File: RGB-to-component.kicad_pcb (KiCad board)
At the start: 2 copper layers, 50 x 70 mm, 59 parts, among them J1 VGA, J3 USB_C_Receptacle_Power, J4 SCART_CONN, J5 3xRCA_CONN, U1 SC6206B-65K5, U2 THS7374, U3 RS8752XK, U6 74AHCT1G86, U7 74AHCT1G86, U8 LM1881

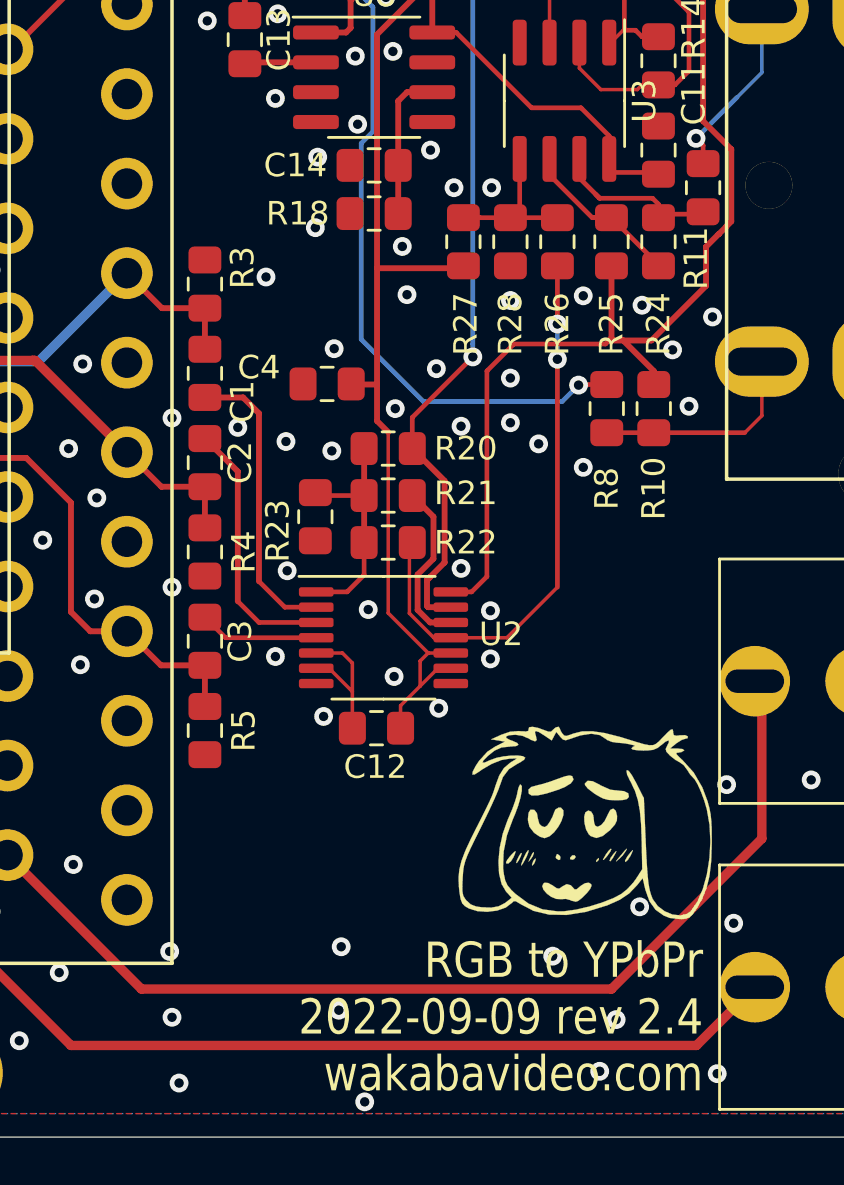
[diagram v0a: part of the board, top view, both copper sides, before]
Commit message: swapping video amps again to TPF141 for JLC availability
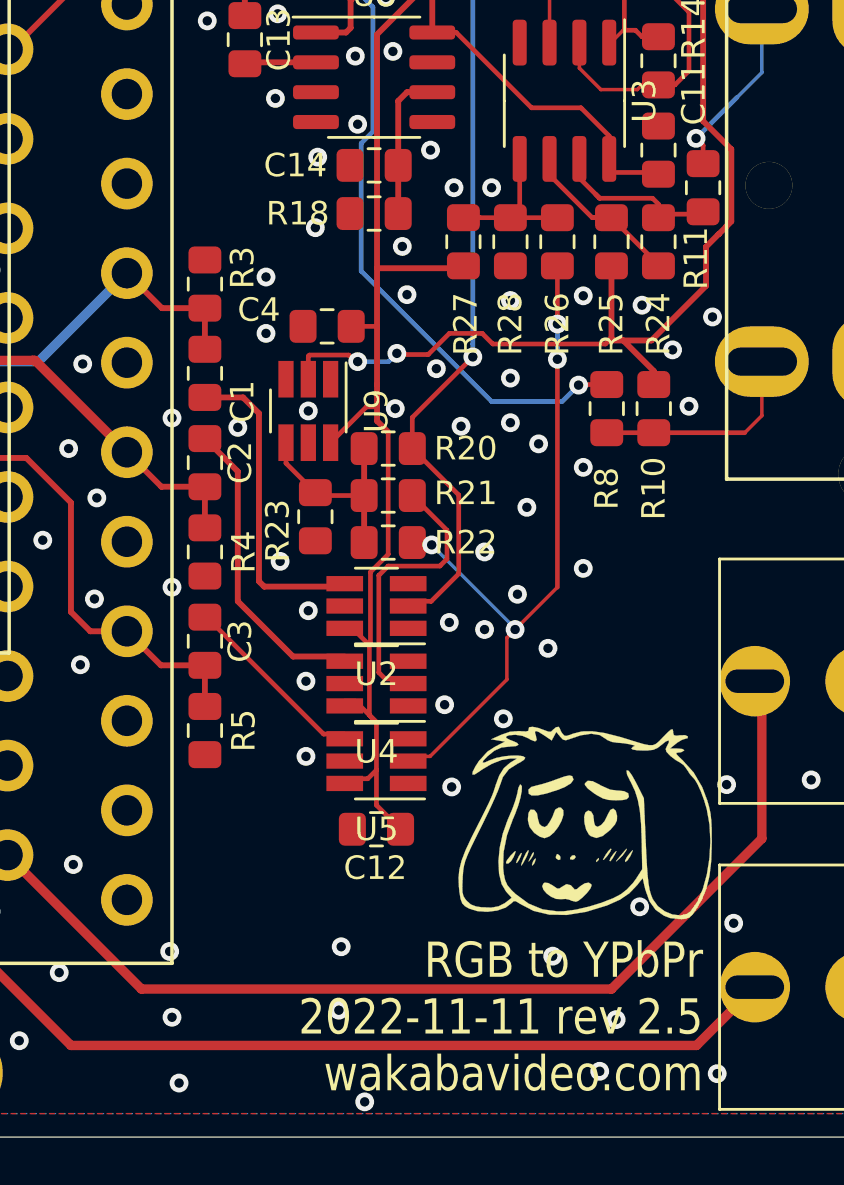
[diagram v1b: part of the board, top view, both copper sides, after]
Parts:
- added U4: TPF141-TR, Package_TO_SOT_SMD:SOT-23-6_Handsoldering, F.Cu at (45.0, 90.7)
- added U5: TPF141-TR, Package_TO_SOT_SMD:SOT-23-6_Handsoldering, F.Cu at (45.0, 94.0)
- added U9: TPF141-TR, Package_TO_SOT_SMD:SOT-23-6_Handsoldering, F.Cu at (42.1, 79.1)
- U2: value THS7374 -> TPF141-TR; footprint Package_SO:TSSOP-14_4.4x5mm_P0.65mm -> Package_TO_SOT_SMD:SOT-23-6_Handsoldering
- moved C12 4.30 mm to (45.0, 96.9)
- moved C4 2.45 mm to (42.9, 75.5)
- moved U2 1.38 mm to (45.0, 87.4), turned to 180 degrees
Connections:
- U2 pad 1: Net-(R20-Pad1) -> (no net)
- U2 pad 2: Net-(C1-Pad1) -> /2R
- U2 pad 3: Net-(C2-Pad1) -> (no net)
- U2 pad 4: Net-(C3-Pad1) -> Net-(C1-Pad1)
- U2 pad 6: GND -> VCC
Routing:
- net VCC: track 110.5 -> 119.6 mm
- net GND: track 5.89 -> 0.00 mm, vias 104 -> 108
- net /2B: track 24.4 -> 30.2 mm, vias 2 -> 4
- net /2G: track 7.15 -> 12.0 mm
- net Net-(C3-Pad1): track 5.10 -> 8.01 mm
- net Net-(C2-Pad1): track 11.2 -> 13.0 mm
- net /SYNC: track 32.9 -> 31.2 mm
- net /2Y: track 44.4 -> 42.8 mm, vias 0 -> 2
- net Net-(R20-Pad1): track 9.84 -> 8.77 mm
- net Net-(C1-Pad1): track 12.6 -> 13.6 mm
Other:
- board text added: "RGB to YPbPr 2022-11-11 rev 2.5 wakabavideo.com"
- board text removed: "RGB to YPbPr 2022-09-09 rev 2.4 wakabavideo.com"

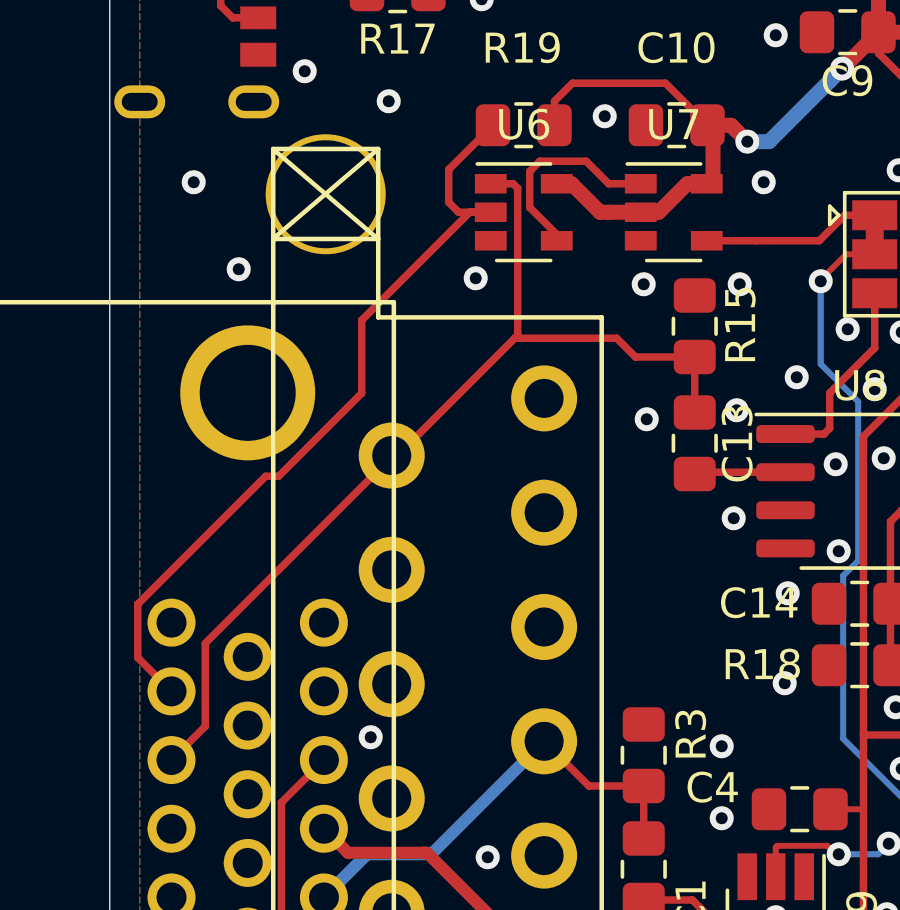
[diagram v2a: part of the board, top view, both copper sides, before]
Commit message: 75 ohm removed from hsync, only terminates scart's csync
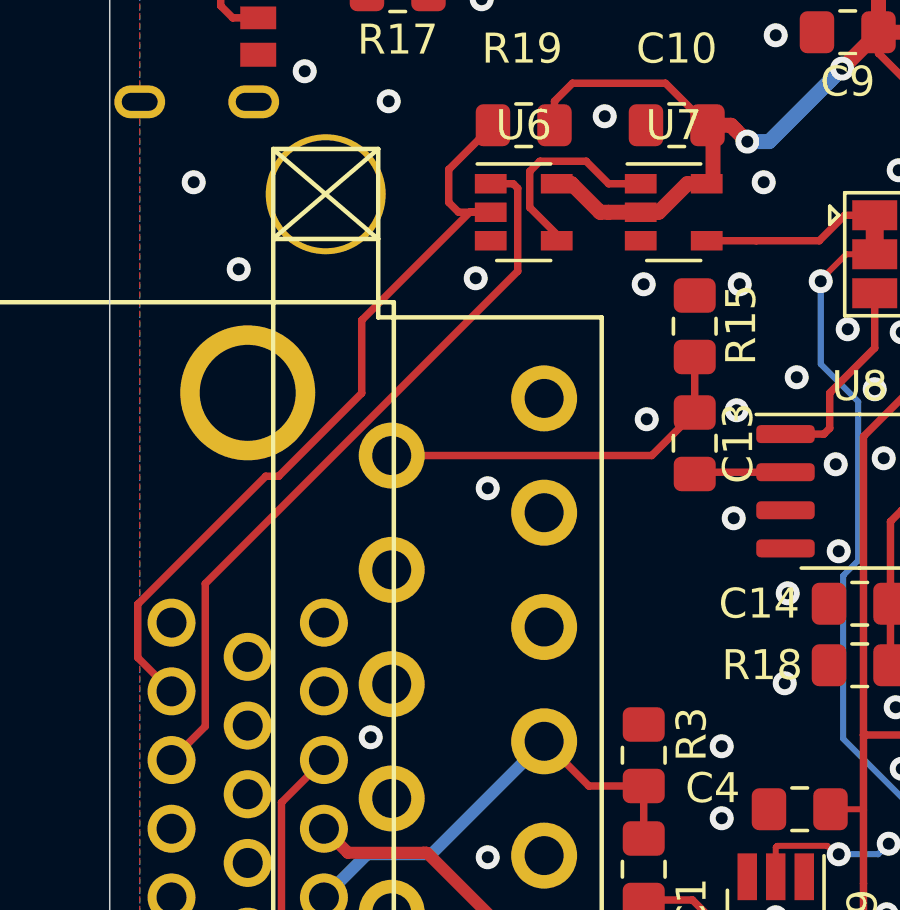
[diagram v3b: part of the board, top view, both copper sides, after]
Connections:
- C13 pad 1: /HSYNC -> /CSYNC
- J4 pad 20: /HSYNC -> /CSYNC
- R15 pad 1: /HSYNC -> /CSYNC
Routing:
- net /CSYNC: track 0.00 -> 12.7 mm
- net /HSYNC: track 33.3 -> 25.0 mm
- net GND: vias 108 -> 109

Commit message: buffer csync stripper, logic moved to single chip
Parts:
- removed U6, U7: 74AHCT1G86, Package_TO_SOT_SMD:SOT-23-5
- added U10: 74HC86, Package_SO:TSSOP-14_4.4x5mm_P0.65mm, F.Cu at (36.8, 53.4)
- moved C10 5.08 mm to (35.8, 48.6), turned to 0 degrees
- moved JP1 2.76 mm to (43.4, 55.1)
- moved R19 1.00 mm to (33.1, 53.5), turned to -90 degrees
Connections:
- JP1 pad 2: /SYNC -> Net-(JP1-C)
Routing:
- net Net-(JP1-C): track 0.00 -> 11.6 mm
- net /SYNC: track 31.2 -> 39.5 mm
- net Net-(U6-Pad4): track 6.71 -> 0.00 mm
- net Net-(U10-Pad3): track 0.00 -> 2.77 mm
- net VCC: track 119.6 -> 122.2 mm, vias 2 -> 1
- net /VGA_CSYNC: track 5.74 -> 8.20 mm
- net /STRIP_CSYNC: track 6.68 -> 7.96 mm
- net /VSYNC: track 26.3 -> 25.5 mm
- net GND: vias 109 -> 108
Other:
- board text added: "RGB to YPbPr 2024-05-22 rev 2.6 wakabavideo.com"
- board text removed: "RGB to YPbPr 2022-11-11 rev 2.5 wakabavideo.com"

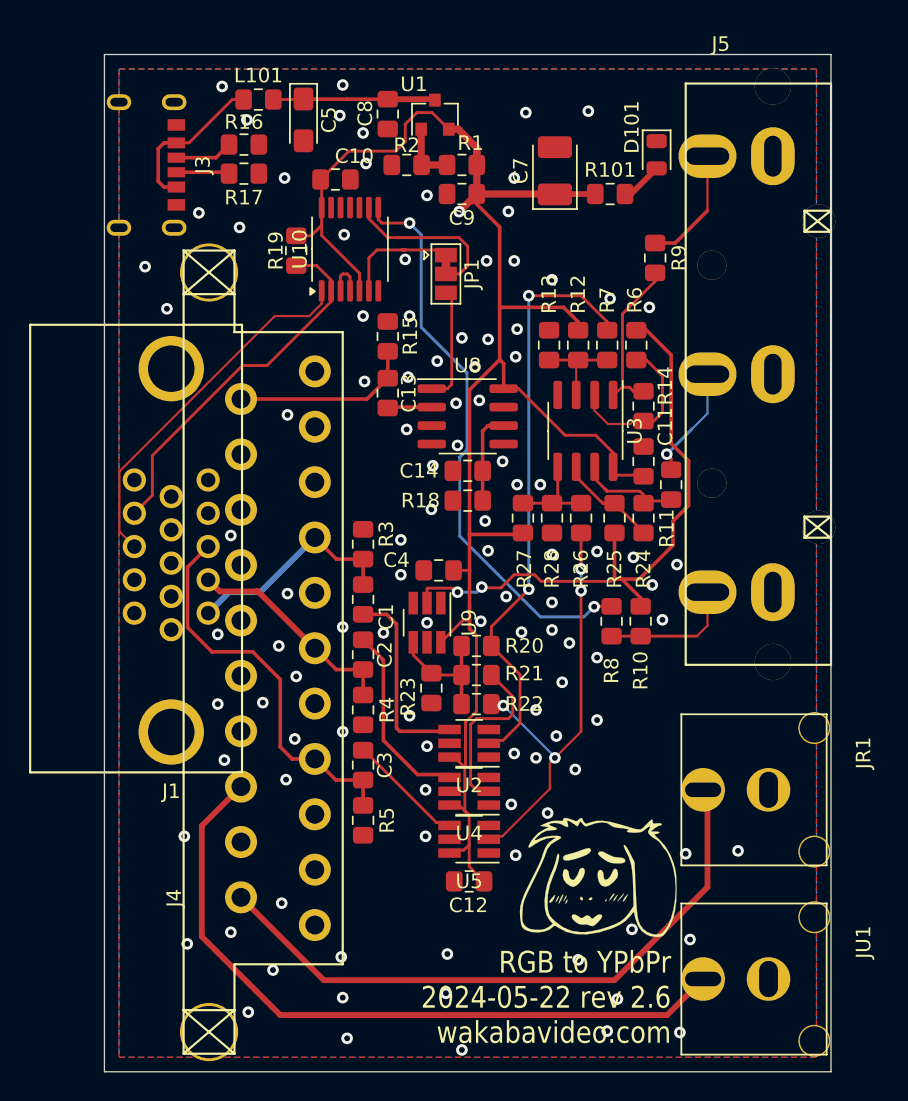
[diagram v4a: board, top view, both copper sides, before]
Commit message: change back to THS7374
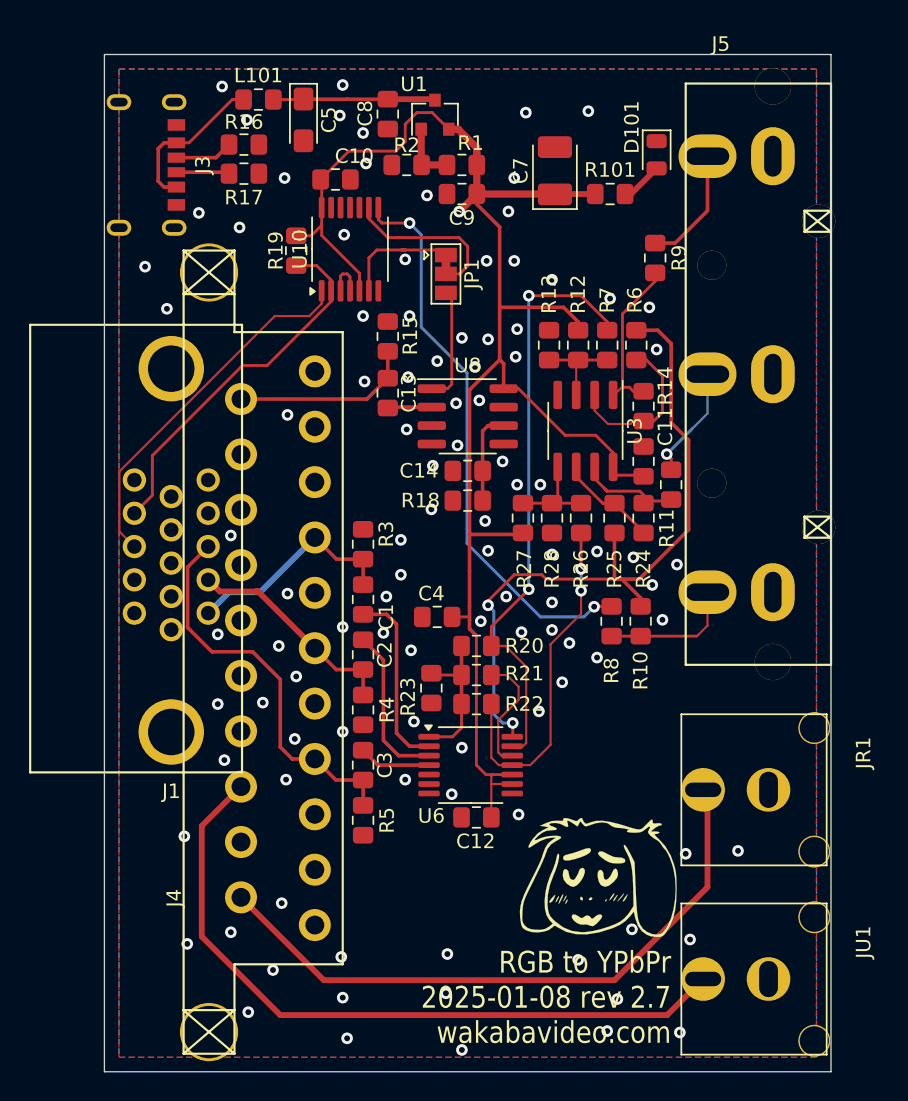
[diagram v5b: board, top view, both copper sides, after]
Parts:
- removed U2, U4, U5, U9: TPF141-TR, Package_TO_SOT_SMD:SOT-23-6_Handsoldering
- added U6: THS7374, Package_SO:TSSOP-14_4.4x5mm_P0.65mm, F.Cu at (45.1, 88.9)
- moved C12 4.43 mm to (45.5, 92.5)
- moved C4 3.20 mm to (42.8, 78.7)
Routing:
- net /2B: track 30.2 -> 24.2 mm, vias 4 -> 2
- net VCC: track 122.2 -> 116.5 mm
- net /2Y: track 42.8 -> 48.1 mm
- net /2G: track 12.0 -> 8.37 mm
- net Net-(U6-CH4_IN): track 8.01 -> 5.04 mm
- net Net-(U6-CH3_IN): track 13.0 -> 11.1 mm
- net Net-(U6-CH1_IN): track 8.77 -> 10.2 mm
- net Net-(U6-CH2_IN): track 13.6 -> 12.7 mm
- net /2R: track 40.7 -> 41.2 mm
- net GND: vias 108 -> 103
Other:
- board text added: "RGB to YPbPr 2025-01-08 rev 2.7 wakabavideo.com"
- board text removed: "RGB to YPbPr 2024-05-22 rev 2.6 wakabavideo.com"

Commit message: swap to THS7374, updated parts
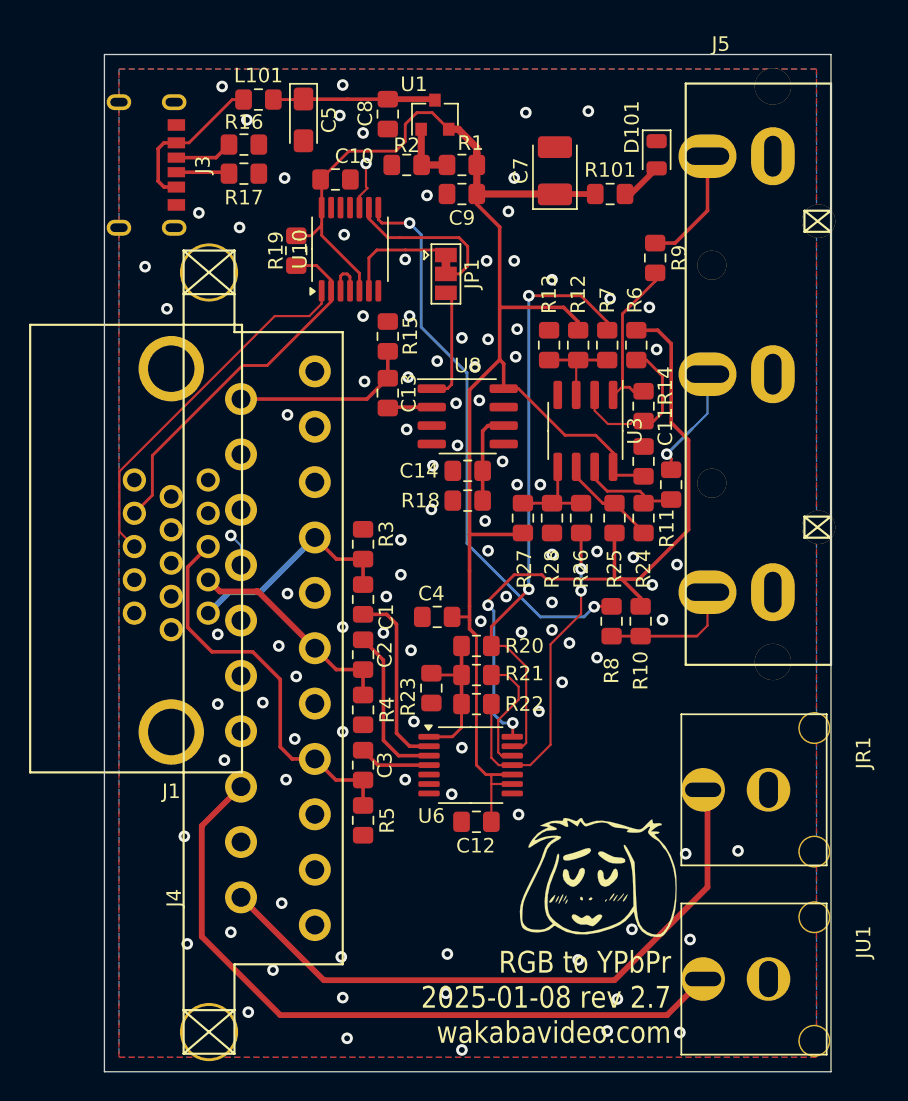
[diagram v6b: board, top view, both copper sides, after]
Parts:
- L101: value 10u -> 10uH
- moved C12 0.30 mm to (45.5, 92.8)
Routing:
- net GND: track 0.00 -> 5.64 mm
- net VCC: track 116.5 -> 114.8 mm, vias 1 -> 0
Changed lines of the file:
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@@
 			)
 		)
-		(property "LCSC" "C20638"
+		(property "LCSC" "C17820"
 			(at 0 0 0)
 			(layer "F.Fab")
@@
 			)
 		)
-		(property "LCSC" " C16133"
+		(property "LCSC" "C16133"
 			(at 0 0 0)
 			(layer "F.Fab")
@@
 			)
 		)
-		(property "LCSC" "C20638"
+		(property "LCSC" "C17820"
 			(at 0 0 0)
 			(layer "F.Fab")
@@
 			)
 		)
-		(property "LCSC" "C20638"
+		(property "LCSC" "C17820"
 			(at 0 0 0)
 			(layer "F.Fab")
@@
 	(footprint "Capacitor_SMD:C_0805_2012Metric_Pad1.15x1.40mm_HandSolder"
 		(layer "F.Cu")
-		(at 45.5 92.5 180)
+		(at 45.5 92.8 180)
 		(descr "Capacitor SMD 0805 (2012 Metric), square (rectangular) end terminal, IPC_7351 nominal with elongated pad for handsoldering. (Body size source: https://docs.google.com/spreadsheets/d/1BsfQQcO9C6DZCsRaXUlFlo91Tg2WpOkGARC1WS5S8t0/edit?usp=sharing), generated with kicad-footprint-generator")
 		(tags "capacitor handsolder")
@@
 			)
 		)
-		(property "LCSC" "C20638"
+		(property "LCSC" "C17820"
 			(at 0 0 0)
 			(layer "F.Fab")
@@
 			)
 		)
-		(property "Datasheet" " ~"
+		(property "Datasheet" ""
 			(at 0 0 -90)
 			(unlocked yes)
@@
 			)
 		)
-		(property "Datasheet" " ~"
+		(property "Datasheet" ""
 			(at 0 0 -90)
 			(unlocked yes)
@@
 			)
 		)
-		(property "LCSC" "C273884"
+		(property "LCSC" "C17736"
 			(at 0 0 0)
 			(layer "F.Fab")
@@
 			)
 		)
-		(property "LCSC" "C26009"
+		(property "LCSC" "C322392"
 			(at 0 0 0)
 			(layer "F.Fab")
@@
 			)
 		)
-		(property "LCSC" "C40880"
+		(property "LCSC" "C101451"
 			(at 0 0 0)
 			(layer "F.Fab")
@@
 			)
 		)
-		(property "LCSC" "C40880"
+		(property "LCSC" "C101451"
 			(at 0 0 0)
 			(layer "F.Fab")
@@
 			)
 		)
-		(property "LCSC" "C20638"
+		(property "LCSC" "C17820"
 			(at 0 0 0)
 			(layer "F.Fab")
@@
 			)
 		)
-		(property "LCSC" "C20638"
+		(property "LCSC" "C17820"
 			(at 0 0 0)
 			(layer "F.Fab")
@@
 			)
 		)
-		(property "LCSC" " C16133"
+		(property "LCSC" "C7171"
 			(at 0 0 0)
 			(layer "F.Fab")
@@
 			)
 		)
-		(property "Value" "10u"
+		(property "Value" "10uH"
 			(at 0 1.65 0)
 			(layer "F.Fab")
@@
 			)
 		)
-		(property "LCSC" "C20638"
+		(property "LCSC" "C17820"
 			(at 0 0 0)
 			(layer "F.Fab")
@@
 		(tags "TSSOP SO")
 		(property "Reference" "U6"
-			(at -2.7 3.5 360)
+			(at -2.7 3.5 0)
 			(layer "F.SilkS")
 			(effects
@@
 		)
 		(property "Value" "THS7374"
-			(at 0 3.45 360)
+			(at 0 3.45 0)
 			(layer "F.Fab")
 			(effects
@@
 		)
 		(fp_text user "${REFERENCE}"
-			(at 0 0 360)
+			(at 0 0 0)
 			(layer "F.Fab")
 			(effects
@@
 			)
 		)
-		(property "JLCPCB" "C471866"
-			(at 0 0 0)
+		(property "LCSC" "C471866"
+			(at 0 0 90)
 			(unlocked yes)
 			(layer "F.Fab")
@@
 	)
 	(segment
-		(start 45.525 49.6)
-		(end 44.3125 50.8125)
-		(width 0.5)
-		(layer "F.Cu")
-		(net 4)
-	)
-	(segment
 		(start 51.5 57.4)
 		(end 47.1 57.4)
@@
 		(net 4)
 	)
-	(via
-		(at 44.3125 50.8125)
-		(size 0.8)
-		(drill 0.4)
-		(layers "F.Cu" "B.Cu")
-		(net 4)
-	)
 	(segment
 		(start 37.965 63.71)
@@
 		(net 5)
 	)
+	(segment
+		(start 37.9 49.1)
+		(end 37.9 47.5)
+		(width 0.15)
+		(layer "F.Cu")
+		(net 6)
+	)
+	(segment
+		(start 37.45 49.75)
+		(end 38 49.2)
+		(width 0.15)
+		(layer "F.Cu")
+		(net 6)
+	)
+	(segment
+		(start 37.45 50.5375)
+		(end 37.45 49.75)
+		(width 0.15)
+		(layer "F.Cu")
+		(net 6)
+	)
+	(segment
+		(start 38 49.2)
+		(end 37.9 49.1)
+		(width 0.15)
+		(layer "F.Cu")
+		(net 6)
+	)
 	(via
 		(at 29.7 44.5)
@@
 	)
 	(segment
+		(start 29.3 75.14)
+		(end 29.3 73.8)
+		(width 0.15)
+		(layer "B.Cu")
+		(net 6)
+	)
+	(segment
+		(start 29.3 73.8)
+		(end 28.6 73.1)
+		(width 0.15)
+		(layer "B.Cu")
+		(net 6)
+	)
+	(segment
 		(start 36.625 43.075)
 		(end 39.4 43.075)
@@
 	)
 	(segment
-		(start 40.330761 53.45)
-		(end 40.6 53.45)
-		(width 0.2)
-		(layer "F.Cu")
-		(net 17)
-	)
-	(segment
 		(start 38.1 56.2625)
 		(end 38.1 54)
@@
 	)
 	(segment
-		(start 54.325 69.875)
-		(end 54.49999 70.04999)
-		(width 0.2)
-		(layer "F.Cu")
-		(net 44)
-	)
-	(segment
 		(start 54.49999 70.04999)
 		(end 56.74999 70.04999)
@@
 		(width 0.2)
 		(layer "F.Cu")
-		(net 50)
-	)
-	(segment
-		(start 40.040001 52.6)
-		(end 40.2 52.6)
-		(width 0.2)
-		(layer "F.Cu")
